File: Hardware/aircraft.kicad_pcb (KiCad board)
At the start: 4 copper layers, 100 x 50 mm, 192 parts, among them J1 Conn_01x02_Pin, J10 Conn_01x06, J12 Conn_02x05_Odd_Even, J13 Conn_01x02, J14 USB_B_Micro, J15 Conn_02x05_Odd_Even, J16 USB_B_Micro, J17 USB_B_Micro, J18 USB_B_Micro, J19 U.FL-R-SMT-1_80_, J2 DM3AT-SF-PEJM5, J3 Conn_01x04, J4 Conn_01x04, J5 Conn_01x10, J6 Conn_02x10_Odd_Even, J7 Conn_01x04, J8 Conn_01x04, J9 Conn_02x06_Odd_Even, SW1 SW_SPDT, SW2 SW_Push_Dual, SW3 SW_SPDT, SW4 SW_Push_Dual, U1 MIC26903YJL-TR, U10 BMP390, U11 W25N01GVZEIG_TR, U12 STM32F405RGTx, U13 W25N01GVZEIG_TR, U14 24CW1280T-I/OT, U15 PCA9685PW_118, U16 CH330N, U17 CH330N, U2 LD39200PU33R, U3 INA226, U4 STM32F405RGTx, U5 IST8310, U6 NEO-M8N, U7 BMI088, U8 TMP100, U9 24CW1280T-I/OT, Y1 25MHz, Y2 25MHz

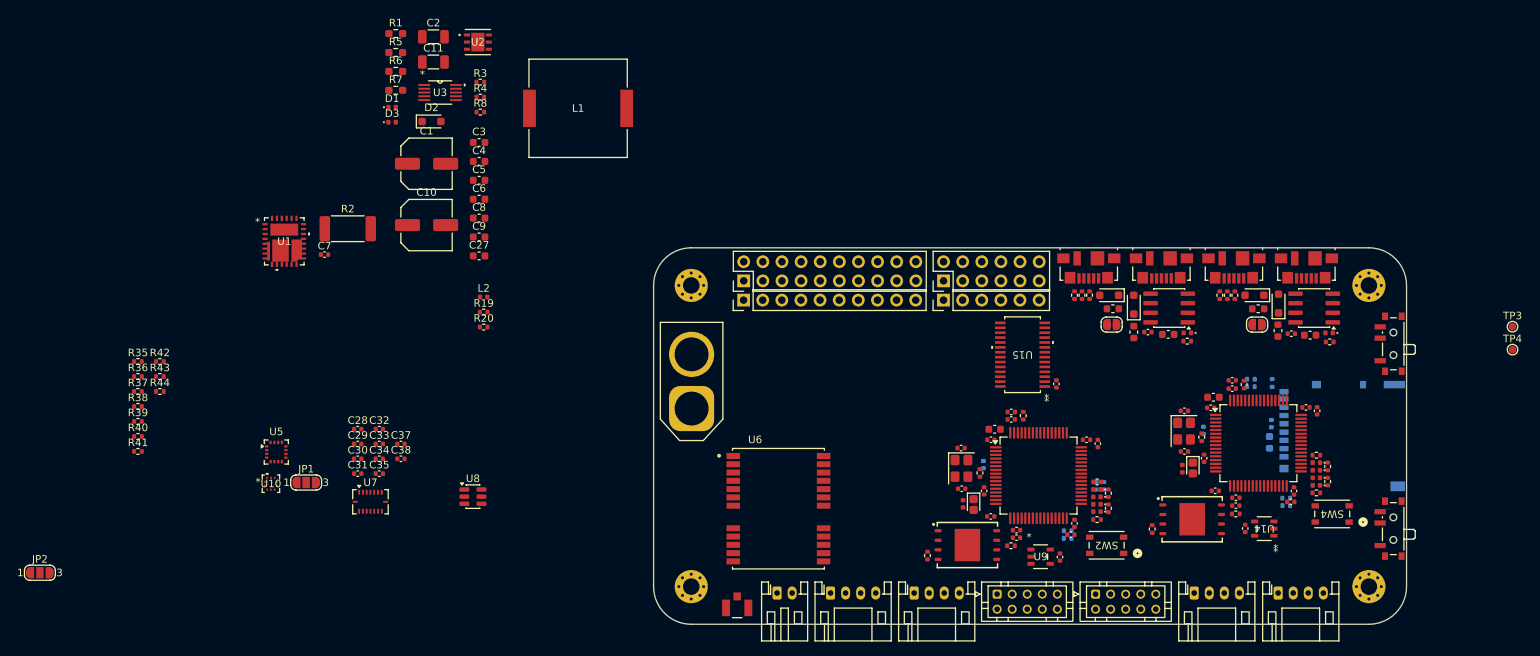
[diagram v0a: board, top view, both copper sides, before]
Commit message: hardware: initial power supply layout
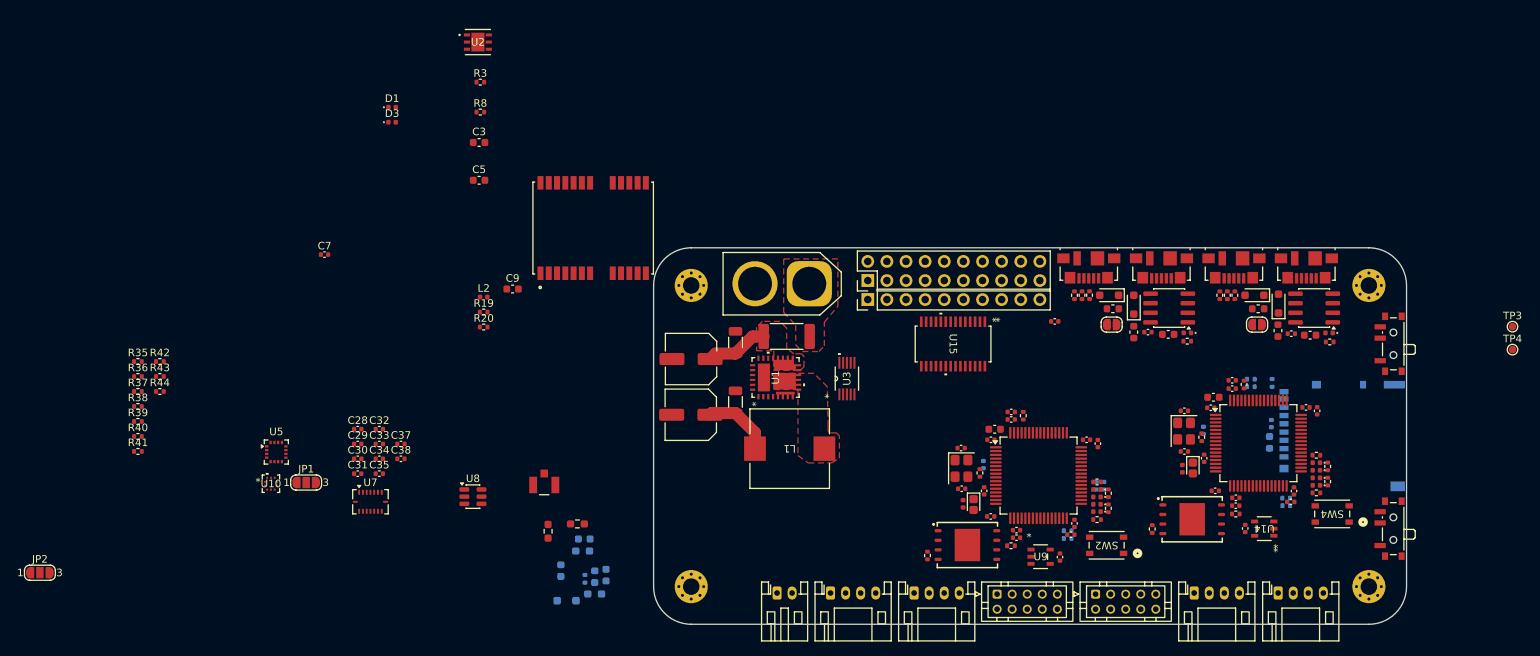
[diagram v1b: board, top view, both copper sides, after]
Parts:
- removed J10: Conn_01x06, Connector_PinHeader_2.54mm:PinHeader_1x06_P2.54mm_Vertical
- removed J9: Conn_02x06_Odd_Even, Connector_PinHeader_2.54mm:PinHeader_2x06_P2.54mm_Vertical
- removed R2: 10m, Resistor_SMD:R_2512_6332Metric_Pad1.40x3.35mm_HandSolder
- added R45: 10m, Resistor_SMD:R_2512_6332Metric_Pad1.40x3.35mm_HandSolder, F.Cu at (136.4, 62.5)
- C27, C4, C6, C8, D2, R1, R4, R5: moved to B.Cu
- J5: value Conn_01x10 -> Conn_02x10_Odd_Even; footprint Connector_PinHeader_2.54mm:PinHeader_1x10_P2.54mm_Vertical -> Connector_PinHeader_2.54mm:PinHeader_2x10_P2.54mm_Vertical
- J6: value Conn_02x10_Odd_Even -> Conn_01x10; footprint Connector_PinHeader_2.54mm:PinHeader_2x10_P2.54mm_Vertical -> Connector_PinHeader_2.54mm:PinHeader_1x10_P2.54mm_Vertical
- L1: footprint Aircraft_Footprints:IND_PA4343_FOOTPRINT2_PUL -> Aircraft_Footprints:IND_SRP1038A_BRN
- moved R1 79.0 mm to (110.9, 96.7), turned to 180 degrees
- moved R5 70.7 mm to (109.3, 91.0)
- moved U1 67.7 mm to (134.9, 67.9), turned to 90 degrees
- moved D2 66.1 mm to (107.2, 97.6)
- moved U3 66.1 mm to (144.4, 68.1), turned to 90 degrees
- moved R4 65.5 mm to (109.6, 94.7), turned to -90 degrees
- moved R6 64.3 mm to (104.7, 88.4), turned to 90 degrees
- moved R7 62.4 mm to (108.6, 87.4)
- moved C11 60.4 mm to (129.6, 71.2), turned to 90 degrees
- moved C4 57.5 mm to (112.4, 94.2), turned to -90 degrees
- moved C2 57.1 mm to (129.6, 63.3), turned to 90 degrees
- moved L1 53.2 mm to (136.8, 77.4), turned to 180 degrees
- moved C6 50.5 mm to (106.4, 93.6), turned to 90 degrees
- moved C27 45.3 mm to (110.9, 94.4), turned to 90 degrees
- moved C8 44.8 mm to (109.5, 89.4)
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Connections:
- net VCC renamed VIN+
- J5 pad 1: PWM_0 -> +5V
- J5 pad 10: PWM_9 -> GND
- J5 pad 2: PWM_1 -> GND
- J5 pad 3: PWM_2 -> +5V
- J5 pad 4: PWM_3 -> GND
- J5 pad 5: PWM_4 -> +5V
- J5 pad 6: PWM_5 -> GND
- J5 pad 7: PWM_6 -> +5V
- J5 pad 8: PWM_7 -> GND
- J5 pad 9: PWM_8 -> unconnected-(J5-Pin_9-Pad9)
- J6 pad 1: +5V -> FCU_TIM3_CH1
- J6 pad 10: GND -> PWM_3
- J6 pad 2: GND -> FCU_TIM3_CH2
- J6 pad 3: +5V -> FCU_TIM3_CH3
- J6 pad 4: GND -> FCU_TIM3_CH4
- J6 pad 5: +5V -> FCU_TIM2_CH1
- J6 pad 6: GND -> FCU_TIM2_CH2
- J6 pad 7: +5V -> PWM_0
- J6 pad 8: GND -> PWM_1
- J6 pad 9: +5V -> PWM_2
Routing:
- net +5V: track 0.00 -> 9.29 mm
- net PS_PVIN: track 0.00 -> 8.36 mm
- added copper zone on F.Cu, net PS_CS
- added copper zone on F.Cu, net PS_PVIN
- added copper zone on F.Cu, net VIN+
